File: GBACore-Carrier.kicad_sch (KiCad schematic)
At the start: 2 parts, among them J1 BM24-40DS_2-0.35V_53_, J2 BM24-40DS_2-0.35V_53_

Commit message: Update pinout
V0.99 Pinout (Final?)
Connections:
- net GND: now also J1.31; no longer J2.34, J2.36, J2.38, J2.40
- net IN35: no longer J1.31
- new net CK1: J2.38
- new net CK2: J2.36

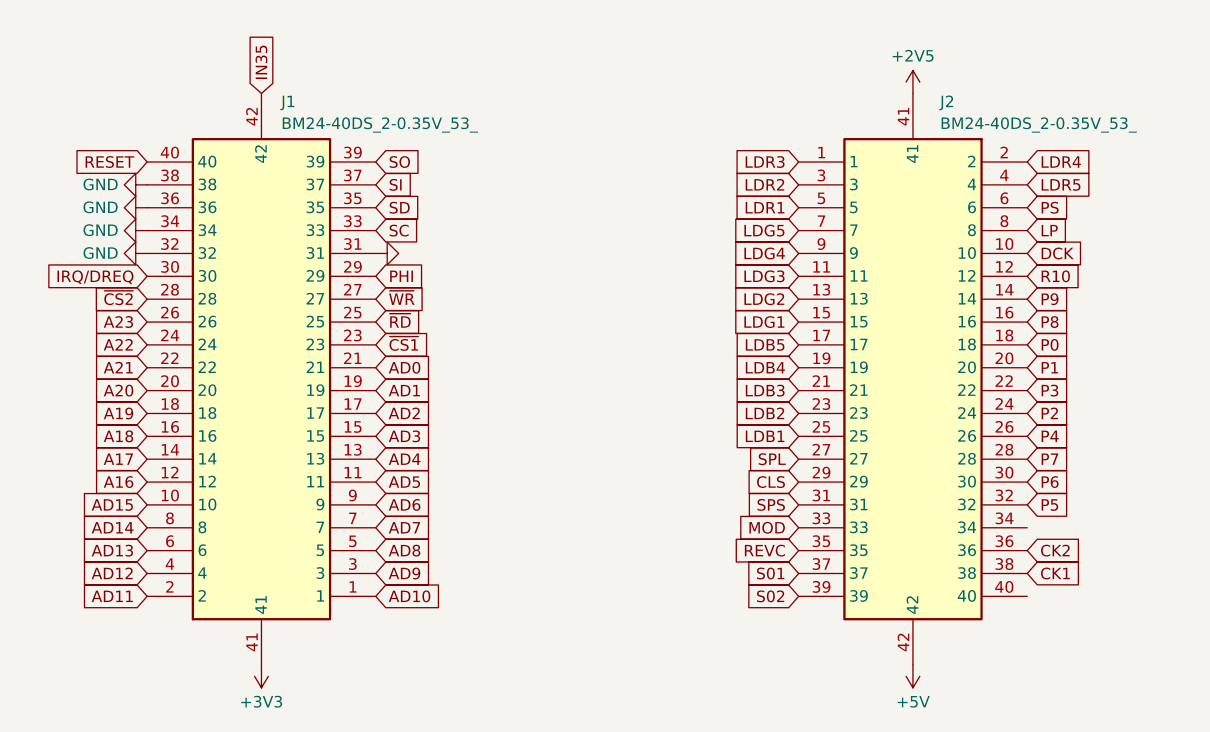
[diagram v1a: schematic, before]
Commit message: Fix orientation of J1
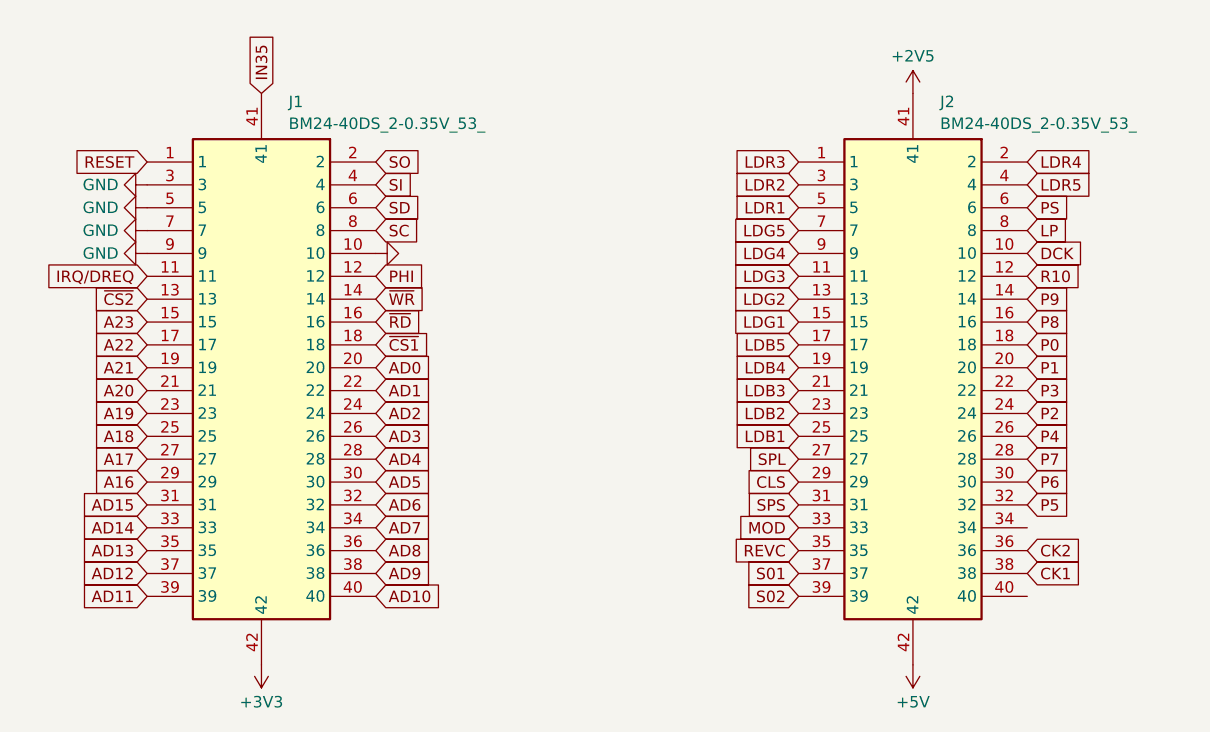
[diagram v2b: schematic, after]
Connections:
- net +3V3: now also J1.42; no longer J1.41
- net A16: now also J1.29; no longer J1.12
- net A17: now also J1.27; no longer J1.14
- net A18: now also J1.25; no longer J1.16
- net A19: now also J1.23; no longer J1.18
- net A20: now also J1.21; no longer J1.20
- net A21: now also J1.19; no longer J1.22
- net A22: now also J1.17; no longer J1.24
- net A23: now also J1.15; no longer J1.26
- net AD0: now also J1.20; no longer J1.21
- net AD1: now also J1.22; no longer J1.19
- net AD10: now also J1.40; no longer J1.1
- net AD11: now also J1.39; no longer J1.2
- net AD12: now also J1.37; no longer J1.4
- net AD13: now also J1.35; no longer J1.6
- net AD14: now also J1.33; no longer J1.8
- net AD15: now also J1.31; no longer J1.10
- net AD2: now also J1.24; no longer J1.17
- net AD3: now also J1.26; no longer J1.15
- net AD4: now also J1.28; no longer J1.13
- net AD5: now also J1.30; no longer J1.11
- net AD6: now also J1.32; no longer J1.9
- net AD7: now also J1.34; no longer J1.7
- net AD8: now also J1.36; no longer J1.5
- net AD9: now also J1.38; no longer J1.3
- net GND: now also J1.10, J1.3, J1.5, J1.7, J1.9; no longer J1.31, J1.32, J1.34, J1.36, J1.38
- net IN35: now also J1.41; no longer J1.42
- net IRQ/DREQ: now also J1.11; no longer J1.30
- net PHI: now also J1.12; no longer J1.29
- net RESET: now also J1.1; no longer J1.40
- net SC: now also J1.8; no longer J1.33
- net SD: now also J1.6; no longer J1.35
- net SI: now also J1.4; no longer J1.37
- net SO: now also J1.2; no longer J1.39
- net ~{CS1}: now also J1.18; no longer J1.23
- net ~{CS2}: now also J1.13; no longer J1.28
- net ~{RD}: now also J1.16; no longer J1.25
- net ~{WR}: now also J1.14; no longer J1.27
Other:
- moved on the sheet: J1
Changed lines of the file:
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@@
 		(lib_name "BM24-40DS_2-0.35V_53__1")
 		(lib_id "BM24-40:BM24-40DS_2-0.35V_53_")
-		(at 72.39 123.19 90)
+		(at 72.39 59.69 270)
 		(unit 1)
 		(exclude_from_sim no)
@@
 		(fields_autoplaced yes)
 		(property "Reference" "J1"
-			(at 74.5841 60.6255 90)
+			(at 75.4065 60.6255 90)
 			(effects
 				(font
 					(size 1.27 1.27)
 				)
-				(justify right)
+				(justify left)
 			)
 		)
 		(property "Value" "BM24-40DS_2-0.35V_53_"
-			(at 74.5841 63.0498 90)
+			(at 75.4065 63.0498 90)
 			(effects
 				(font
 					(size 1.27 1.27)
 				)
-				(justify right)
+				(justify left)
 			)
 		)
 		(property "Footprint" "Connector_Hirose:Hirose_BM24_BM24-40DS-2-0.35V_2x20_P0.35mm_PowerPin2_Vertical"
-			(at 162.23 63.5 0)
+			(at -17.45 119.38 0)
 			(effects
 				(font
@@
 		)
 		(property "Datasheet" "https://www.hirose.com/en/product/document?clcode=CL0677-2010-0-53&productname=BM24-40DS%2f2-0.35V(53)&series=BM24&documenttype=2DDrawing&lang=en&documentid=0001166555"
-			(at 262.23 63.5 0)
+			(at -117.45 119.38 0)
 			(effects
 				(font
@@
 		)
 		(property "Description" "CONN SOCKET 40POS SMD GOLD"
-			(at 72.39 123.19 0)
+			(at 72.39 59.69 0)
 			(effects
 				(font
@@
 		)
 		(property "Height" "0.9"
-			(at 462.23 63.5 0)
+			(at -317.45 119.38 0)
 			(effects
 				(font
@@
 		)
 		(property "Manufacturer_Name" "Hirose"
-			(at 562.23 63.5 0)
+			(at -417.45 119.38 0)
 			(effects
 				(font
@@
 		)
 		(property "Manufacturer_Part_Number" "BM24-40DS/2-0.35V(53)"
-			(at 662.23 63.5 0)
+			(at -517.45 119.38 0)
 			(effects
 				(font
@@
 		)
 		(property "Mouser Part Number" "798-BM2440DS20.35V53"
-			(at 762.23 63.5 0)
+			(at -617.45 119.38 0)
 			(effects
 				(font
@@
 		)
 		(property "Mouser Price/Stock" "https://www.mouser.co.uk/ProductDetail/Hirose-Connector/BM24-40DS-2-0.35V53?qs=c8NFF48pVsBxiWngIa8Cog%3D%3D"
-			(at 862.23 63.5 0)
+			(at -717.45 119.38 0)
 			(effects
 				(font
@@
 		)
 		(property "Arrow Part Number" ""
-			(at 962.23 63.5 0)
+			(at -817.45 119.38 0)
 			(effects
 				(font
@@
 		)
 		(property "Arrow Price/Stock" ""
-			(at 1062.23 63.5 0)
+			(at -917.45 119.38 0)
 			(effects
 				(font

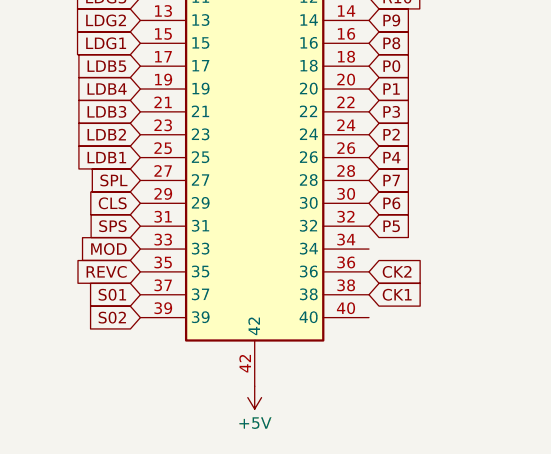
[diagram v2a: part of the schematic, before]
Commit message: Add missing gnd pins
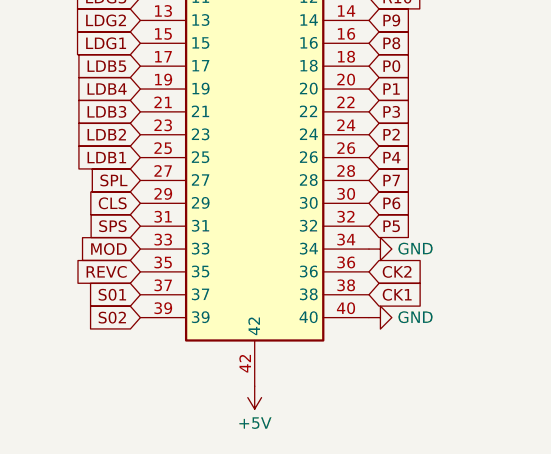
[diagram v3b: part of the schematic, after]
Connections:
- net GND: now also J2.34, J2.40
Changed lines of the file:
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@@
+	(symbol
+		(lib_id "power:GND")
+		(at 157.48 107.95 90)
+		(unit 1)
+		(exclude_from_sim no)
+		(in_bom yes)
+		(on_board yes)
+		(dnp no)
+		(fields_autoplaced yes)
+		(property "Reference" "#PWR01"
+			(at 163.83 107.95 0)
+			(effects
+				(font
+					(size 1.27 1.27)
+				)
+				(hide yes)
+			)
+		)
+		(property "Value" "GND"
+			(at 160.655 107.95 90)
+			(effects
+				(font
+					(size 1.27 1.27)
+				)
+				(justify right)
+			)
+		)
+		(property "Footprint" ""
+			(at 157.48 107.95 0)
+			(effects
+				(font
+					(size 1.27 1.27)
+				)
+				(hide yes)
+			)
+		)
+		(property "Datasheet" ""
+			(at 157.48 107.95 0)
+			(effects
+				(font
+					(size 1.27 1.27)
+				)
+				(hide yes)
+			)
+		)
+		(property "Description" "Power symbol creates a global label with name \"GND\" , ground"
+			(at 157.48 107.95 0)
+			(effects
+				(font
+					(size 1.27 1.27)
+				)
+				(hide yes)
+			)
+		)
+		(pin "1"
+		)
+		(instances
+			(project "GBACore-Carrier"
+				(path "/96ae01f8-5aa4-4c0e-9715-fbc2ab0b7781"
+					(reference "#PWR01")
+					(unit 1)
+				)
+			)
+		)
+	)
 	(symbol
 		(lib_id "power:GND")
@@
 					(unit 1)
 				)
+			)
+		)
+	)
+	(symbol
+		(lib_id "power:GND")
+		(at 157.48 115.57 90)
+		(unit 1)
+		(exclude_from_sim no)
+		(in_bom yes)
+		(on_board yes)
+		(dnp no)
+		(fields_autoplaced yes)
+		(property "Reference" "#PWR02"
+			(at 163.83 115.57 0)
+			(effects
+				(font
+					(size 1.27 1.27)
+				)
+				(hide yes)
+			)
+		)
+		(property "Value" "GND"
+			(at 160.655 115.57 90)
+			(effects
+				(font
+					(size 1.27 1.27)
+				)
+				(justify right)
+			)
+		)
+		(property "Footprint" ""
+			(at 157.48 115.57 0)
+			(effects
+				(font
+					(size 1.27 1.27)
+				)
+				(hide yes)
+			)
+		)
+		(property "Datasheet" ""
+			(at 157.48 115.57 0)
+			(effects
+				(font
+					(size 1.27 1.27)
+				)
+				(hide yes)
+			)
+		)
+		(property "Description" "Power symbol creates a global label with name \"GND\" , ground"
+			(at 157.48 115.57 0)
+			(effects
+				(font
+					(size 1.27 1.27)
+				)
+				(hide yes)
+			)
+		)
+		(pin "1"
+		)
+		(instances
+			(project "GBACore-Carrier"
+				(path "/96ae01f8-5aa4-4c0e-9715-fbc2ab0b7781"
+					(reference "#PWR02")
+					(unit 1)
+				)
